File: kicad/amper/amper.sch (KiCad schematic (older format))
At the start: 54 parts, among them J1 Conn_02x05_Odd_Even, J2 Conn_02x05_Odd_Even, J3 Conn_02x05_Odd_Even, J4 USB_C_Receptacle_USB2.0, J5 Conn_01x03, J6 Conn_01x04, J7 Conn_01x05, Q1 FDS9435A, Q2 FDS9435A, SW1 SW_Push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

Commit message: misc corrections
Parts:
- J4: symbol Connector:USB_C_Receptacle_USB2.0 -> amper-symbols:USB_C_Receptacle_USB2.0_shield
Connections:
- no-connect marks 22 -> 25
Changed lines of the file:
@@
 L power:GND #PWR016
 U 1 1 6234E5E5
-P 9050 5200
-F 0 "#PWR016" H 9050 4950 50  0001 C CNN
-F 1 "GND" H 9055 5027 50  0000 C CNN
-F 2 "" H 9050 5200 50  0001 C CNN
-F 3 "" H 9050 5200 50  0001 C CNN
-	1    9050 5200
-	1    0    0    -1
-$EndComp
-Wire Wire Line
-	9050 5200 9050 5100
+P 9150 5200
+F 0 "#PWR016" H 9150 4950 50  0001 C CNN
+F 1 "GND" H 9155 5027 50  0000 C CNN
+F 2 "" H 9150 5200 50  0001 C CNN
+F 3 "" H 9150 5200 50  0001 C CNN
+	1    9150 5200
+	1    0    0    -1
+$EndComp
+Wire Wire Line
+	9150 5200 9150 5100
 $Comp
 L Device:CP1 C5
@@
 NoConn ~ 9650 4300
 $Comp
-L Connector:USB_C_Receptacle_USB2.0 J4
+L amper-symbols:USB_C_Receptacle_USB2.0_shield J4
 U 1 1 626A33B5
 P 9050 4200
@@
 Wire Wire Line
 	1400 2000 1400 2100
+NoConn ~ 8850 5100
+NoConn ~ 8950 5100
+NoConn ~ 9050 5100
 $EndSCHEMATC

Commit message: almost finished first path at board rev b, still a little work to do around logos, text and plane continuity
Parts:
- added J8, J9: Conn_01x09, Connector_PinSocket_2.54mm:PinSocket_1x09_P2.54mm_Vertical, symbol Connector_Generic:Conn_01x09
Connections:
- net AtProg: now also J9.4 (Pin_4)
- net ResultAdc: now also J8.7 (Pin_7)
- net SourceADn: now also J9.7 (Pin_7)
- net SourceAOut: now also J9.3 (Pin_3)
- net SourceAPwm: now also J9.1 (Pin_1)
- net SourceAUp: now also J9.8 (Pin_8)
- net SourceBDn: now also J9.5 (Pin_5)
- net SourceBOut: now also J9.2 (Pin_2)
- net SourceBPwm: now also J9.9 (Pin_9)
- net SourceBUp: now also J9.6 (Pin_6)
- net Tm1637Clk: now also J8.9 (Pin_9)
- net Tm1637Dio: now also J8.8 (Pin_8)
- net UartRx: now also J8.3 (Pin_3)
- net UartTx: now also J8.2 (Pin_2)
- net at U7.10 (PB1): now also J8.1 (Pin_1)
- net at U7.5 (PA7): now also J8.6 (Pin_6)
- net at U7.6 (PB5): now also J8.5 (Pin_5)
- net at U7.7 (PB4): now also J8.4 (Pin_4)
- no-connect marks 25 -> 21
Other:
- note removed: "Expose these traces\nfor ease of bodging"
- moved on the sheet: C12, U7
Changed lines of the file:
@@
 L amper-symbols:ATtiny1606-S U7
 U 1 1 62224E78
-P 9850 2000
-F 0 "U7" H 9850 2965 50  0000 C CNN
-F 1 "ATtiny1606-S" H 9850 2874 50  0000 C CNN
-F 2 "Package_SO:SOIC-20W_7.5x12.8mm_P1.27mm" H 9850 1650 50  0001 C CIN
-F 3 "http://ww1.microchip.com/downloads/en/DeviceDoc/ATtiny806_1606_Data_Sheet_40002029A.pdf" H 9850 2000 50  0001 C CNN
-	1    9850 2000
-	1    0    0    -1
-$EndComp
-Wire Wire Line
-	10450 1300 10550 1300
+P 9300 2000
+F 0 "U7" H 9300 2965 50  0000 C CNN
+F 1 "ATtiny1606-S" H 9300 2874 50  0000 C CNN
+F 2 "Package_SO:SOIC-20W_7.5x12.8mm_P1.27mm" H 9300 1650 50  0001 C CIN
+F 3 "http://ww1.microchip.com/downloads/en/DeviceDoc/ATtiny806_1606_Data_Sheet_40002029A.pdf" H 9300 2000 50  0001 C CNN
+	1    9300 2000
+	1    0    0    -1
+$EndComp
+Wire Wire Line
+	9900 1300 10000 1300
 $Comp
 L power:+5V #PWR017
 U 1 1 622DD6E8
-P 9150 850
-F 0 "#PWR017" H 9150 700 50  0001 C CNN
-F 1 "+5V" H 9165 1023 50  0000 C CNN
-F 2 "" H 9150 850 50  0001 C CNN
-F 3 "" H 9150 850 50  0001 C CNN
-	1    9150 850
-	1    0    0    -1
-$EndComp
-Wire Wire Line
-	9150 1300 9250 1300
+P 8600 850
+F 0 "#PWR017" H 8600 700 50  0001 C CNN
+F 1 "+5V" H 8615 1023 50  0000 C CNN
+F 2 "" H 8600 850 50  0001 C CNN
+F 3 "" H 8600 850 50  0001 C CNN
+	1    8600 850
+	1    0    0    -1
+$EndComp
+Wire Wire Line
+	8600 1300 8700 1300
 $Comp
 L power:GND #PWR022
 U 1 1 622EC3F9
-P 10750 950
-F 0 "#PWR022" H 10750 700 50  0001 C CNN
-F 1 "GND" H 10755 777 50  0000 C CNN
-F 2 "" H 10750 950 50  0001 C CNN
-F 3 "" H 10750 950 50  0001 C CNN
-	1    10750 950
-	1    0    0    -1
-$EndComp
-Wire Wire Line
-	10550 1300 10550 950
-Wire Wire Line
-	10750 850  10750 950
-Text Label 10500 1700 0    50   ~ 0
+P 10200 950
+F 0 "#PWR022" H 10200 700 50  0001 C CNN
+F 1 "GND" H 10205 777 50  0000 C CNN
+F 2 "" H 10200 950 50  0001 C CNN
+F 3 "" H 10200 950 50  0001 C CNN
+	1    10200 950
+	1    0    0    -1
+$EndComp
+Wire Wire Line
+	10000 1300 10000 950
+Wire Wire Line
+	10200 850  10200 950
+Text Label 9950 1700 0    50   ~ 0
 AtProg
-Text Label 10500 1600 0    50   ~ 0
+Text Label 9950 1600 0    50   ~ 0
 SourceAOut
-Text Label 10500 1500 0    50   ~ 0
+Text Label 9950 1500 0    50   ~ 0
 SourceBOut
-Text Label 10500 1400 0    50   ~ 0
+Text Label 9950 1400 0    50   ~ 0
 SourceAPwm
-Text Label 9200 1400 2    50   ~ 0
+Text Label 8650 1400 2    50   ~ 0
 Tm1637Clk
-Text Label 9200 1500 2    50   ~ 0
+Text Label 8650 1500 2    50   ~ 0
 Tm1637Dio
-Text Label 9200 1600 2    50   ~ 0
+Text Label 8650 1600 2    50   ~ 0
 ResultAdc
-Text Label 10500 2200 0    50   ~ 0
+Text Label 9950 2200 0    50   ~ 0
 SourceBPwm
-Text Label 9150 2100 2    50   ~ 0
+Text Label 8600 2100 2    50   ~ 0
 UartTx
-Text Label 9150 2000 2    50   ~ 0
+Text Label 8600 2000 2    50   ~ 0
 UartRx
-Text Label 10500 2100 0    50   ~ 0
+Text Label 9950 2100 0    50   ~ 0
 SourceAUp
-Text Label 10500 2000 0    50   ~ 0
+Text Label 9950 2000 0    50   ~ 0
 SourceADn
-Text Label 10500 1900 0    50   ~ 0
+Text Label 9950 1900 0    50   ~ 0
 SourceBUp
-Text Label 10500 1800 0    50   ~ 0
+Text Label 9950 1800 0    50   ~ 0
 SourceBDn
 $Comp
@@
 Wire Wire Line
 	10600 4650 10700 4650
-Wire Wire Line
-	9150 2100 9250 2100
-Wire Wire Line
-	9150 2000 9250 2000
-Wire Wire Line
-	9200 1400 9250 1400
-Wire Wire Line
-	9200 1500 9250 1500
-Wire Wire Line
-	9200 1600 9250 1600
-NoConn ~ 9250 1700
-NoConn ~ 9250 1800
-NoConn ~ 9250 1900
-NoConn ~ 9250 2200
-Wire Wire Line
-	10450 1400 10500 1400
-Wire Wire Line
-	10450 1500 10500 1500
-Wire Wire Line
-	10500 1600 10450 1600
-Wire Wire Line
-	10450 1700 10500 1700
-Wire Wire Line
-	10500 1800 10450 1800
-Wire Wire Line
-	10450 1900 10500 1900
-Wire Wire Line
-	10500 2000 10450 2000
-Wire Wire Line
-	10450 2100 10500 2100
-Wire Wire Line
-	10500 2200 10450 2200
-Text Notes 9100 2650 0    100  ~ 0
-Expose these traces\nfor ease of bodging
-Wire Notes Line
-	11000 2700 8750 2700
-Wire Notes Line
-	8750 550  11000 550
 $Comp
 L Connector_Generic:Conn_01x05 J7
@@
 Wire Wire Line
 	10700 5600 10050 5600
-Text Notes 850  4850 0    100  ~ 0
-Expose these traces\nfor ease of bodging
 $Comp
 L power:+5V #PWR018
@@
 Wire Wire Line
 	4250 4500 4550 4500
-Wire Notes Line
-	700  4400 4750 4400
-Wire Notes Line
-	700  6250 4750 6250
-Wire Notes Line
-	4750 4400 4750 6250
-Wire Notes Line
-	700  4400 700  6250
 $Comp
 L Connector_Generic:Conn_02x05_Odd_Even J3
@@
 L Device:C C12
 U 1 1 62E8013E
-P 10300 950
-F 0 "C12" V 10048 950 50  0000 C CNN
-F 1 "100n" V 10139 950 50  0000 C CNN
-F 2 "Capacitor_SMD:C_0603_1608Metric_Pad1.05x0.95mm_HandSolder" H 10338 800 50  0001 C CNN
-F 3 "~" H 10300 950 50  0001 C CNN
-	1    10300 950
+P 9750 950
+F 0 "C12" V 9498 950 50  0000 C CNN
+F 1 "100n" V 9589 950 50  0000 C CNN
+F 2 "Capacitor_SMD:C_0603_1608Metric_Pad1.05x0.95mm_HandSolder" H 9788 800 50  0001 C CNN
+F 3 "~" H 9750 950 50  0001 C CNN
+	1    9750 950
 	0    1    1    0
 $EndComp
 Wire Wire Line
-	10550 850  10750 850
-Wire Wire Line
-	10450 950  10550 950
-Connection ~ 10550 950
-Wire Wire Line
-	10550 950  10550 850
-Wire Wire Line
-	10150 950  9150 950
-Wire Wire Line
-	9150 950  9150 1300
-Wire Wire Line
-	9150 950  9150 850
-Connection ~ 9150 950
-Wire Notes Line
-	8750 550  8750 2700
-Wire Notes Line
-	11000 550  11000 2700
+	10000 850  10200 850
+Wire Wire Line
+	9900 950  10000 950
+Connection ~ 10000 950
+Wire Wire Line
+	10000 950  10000 850
+Wire Wire Line
+	9600 950  8600 950
+Wire Wire Line
+	8600 950  8600 1300
+Wire Wire Line
+	8600 950  8600 850
+Connection ~ 8600 950
 Wire Wire Line
 	1000 3250 1400 3250
@@
 NoConn ~ 8950 5100
 NoConn ~ 9050 5100
+$Comp
+L Connector_Generic:Conn_01x09 J8
+U 1 1 634F05AF
+P 8000 1800
+F 0 "J8" H 8000 1150 50  0000 C CNN
+F 1 "Conn_01x09" H 8000 1250 50  0000 C CNN
+F 2 "Connector_PinSocket_2.54mm:PinSocket_1x09_P2.54mm_Vertical" H 8000 1800 50  0001 C CNN
+F 3 "~" H 8000 1800 50  0001 C CNN
+	1    8000 1800
+	-1   0    0    1
+$EndComp
+Wire Wire Line
+	8200 1400 8700 1400
+Wire Wire Line
+	8200 1500 8700 1500
+Wire Wire Line
+	8200 1600 8700 1600
+Wire Wire Line
+	8200 2000 8700 2000
+Wire Wire Line
+	8200 2100 8700 2100
+Wire Wire Line
+	9900 2200 10400 2200
+Wire Wire Line
+	8200 1900 8700 1900
+Wire Wire Line
+	8700 1800 8200 1800
+Wire Wire Line
+	8200 1700 8700 1700
+$Comp
+L Connector_Generic:Conn_01x09 J9
+U 1 1 635FB8AF
+P 10600 1800
+F 0 "J9" H 10600 2450 50  0000 C CNN
+F 1 "Conn_01x09" H 10600 2350 50  0000 C CNN
+F 2 "Connector_PinSocket_2.54mm:PinSocket_1x09_P2.54mm_Vertical" H 10600 1800 50  0001 C CNN
+F 3 "~" H 10600 1800 50  0001 C CNN
+	1    10600 1800
+	1    0    0    -1
+$EndComp
+Wire Wire Line
+	8200 2200 8700 2200
+Wire Wire Line
+	9900 2100 10400 2100
+Wire Wire Line
+	9900 2000 10400 2000
+Wire Wire Line
+	9900 1900 10400 1900
+Wire Wire Line
+	9900 1800 10400 1800
+Wire Wire Line
+	9900 1700 10400 1700
+Wire Wire Line
+	9900 1600 10400 1600
+Wire Wire Line
+	9900 1500 10400 1500
+Wire Wire Line
+	9900 1400 10400 1400
 $EndSCHEMATC

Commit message: rev B as fabbed
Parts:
- J8, J9: footprint Connector_PinSocket_2.54mm:PinSocket_1x09_P2.54mm_Vertical -> amper:PinSocket_1x09_P2.54mm_Vertical_no_silk
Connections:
- net AtProg: now also J9.6 (Pin_6); no longer J9.4 (Pin_4)
- net SourceADn: now also J9.3 (Pin_3); no longer J9.7 (Pin_7)
- net SourceAOut: now also J9.7 (Pin_7); no longer J9.3 (Pin_3)
- net SourceAPwm: now also J9.9 (Pin_9); no longer J9.1 (Pin_1)
- net SourceAUp: now also J9.2 (Pin_2); no longer J9.8 (Pin_8)
- net SourceBOut: now also J9.8 (Pin_8); no longer J9.2 (Pin_2)
- net SourceBPwm: now also J9.1 (Pin_1); no longer J9.9 (Pin_9)
- net SourceBUp: now also J9.4 (Pin_4); no longer J9.6 (Pin_6)
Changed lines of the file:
@@
 F 0 "J8" H 8000 1150 50  0000 C CNN
 F 1 "Conn_01x09" H 8000 1250 50  0000 C CNN
-F 2 "Connector_PinSocket_2.54mm:PinSocket_1x09_P2.54mm_Vertical" H 8000 1800 50  0001 C CNN
+F 2 "amper:PinSocket_1x09_P2.54mm_Vertical_no_silk" H 8000 1800 50  0001 C CNN
 F 3 "~" H 8000 1800 50  0001 C CNN
 	1    8000 1800
@@
 U 1 1 635FB8AF
 P 10600 1800
-F 0 "J9" H 10600 2450 50  0000 C CNN
-F 1 "Conn_01x09" H 10600 2350 50  0000 C CNN
-F 2 "Connector_PinSocket_2.54mm:PinSocket_1x09_P2.54mm_Vertical" H 10600 1800 50  0001 C CNN
+F 0 "J9" H 10600 1150 50  0000 C CNN
+F 1 "Conn_01x09" H 10600 1250 50  0000 C CNN
+F 2 "amper:PinSocket_1x09_P2.54mm_Vertical_no_silk" H 10600 1800 50  0001 C CNN
 F 3 "~" H 10600 1800 50  0001 C CNN
 	1    10600 1800
-	1    0    0    -1
+	1    0    0    1
 $EndComp
 Wire Wire Line

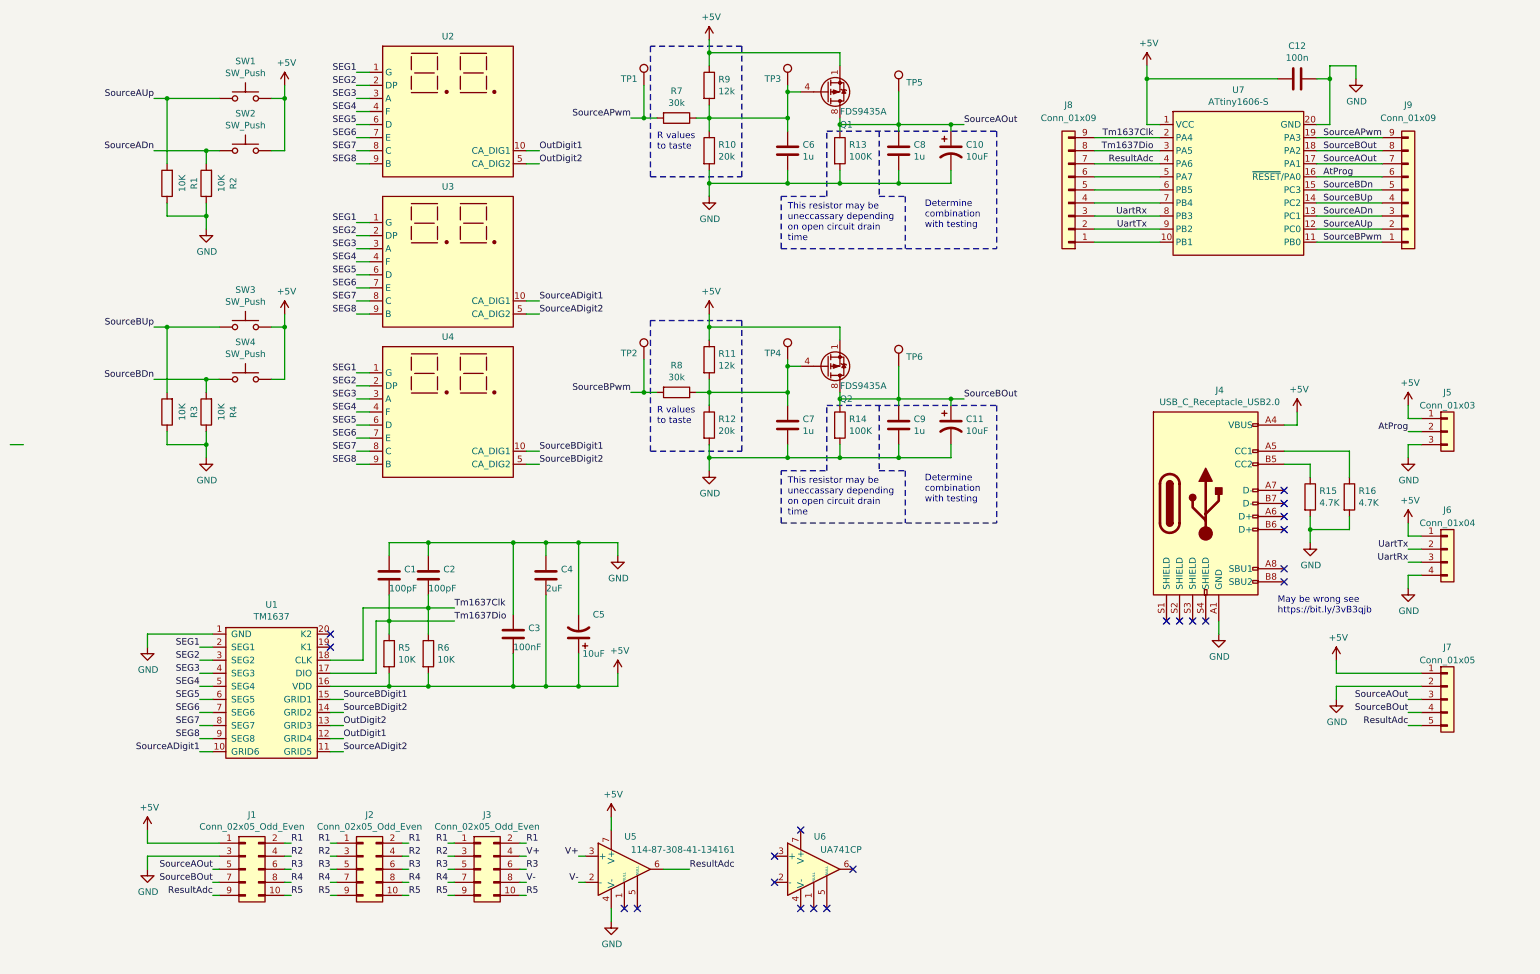
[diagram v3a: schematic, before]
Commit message: Updated power supplies to schematic, reorganised schematic
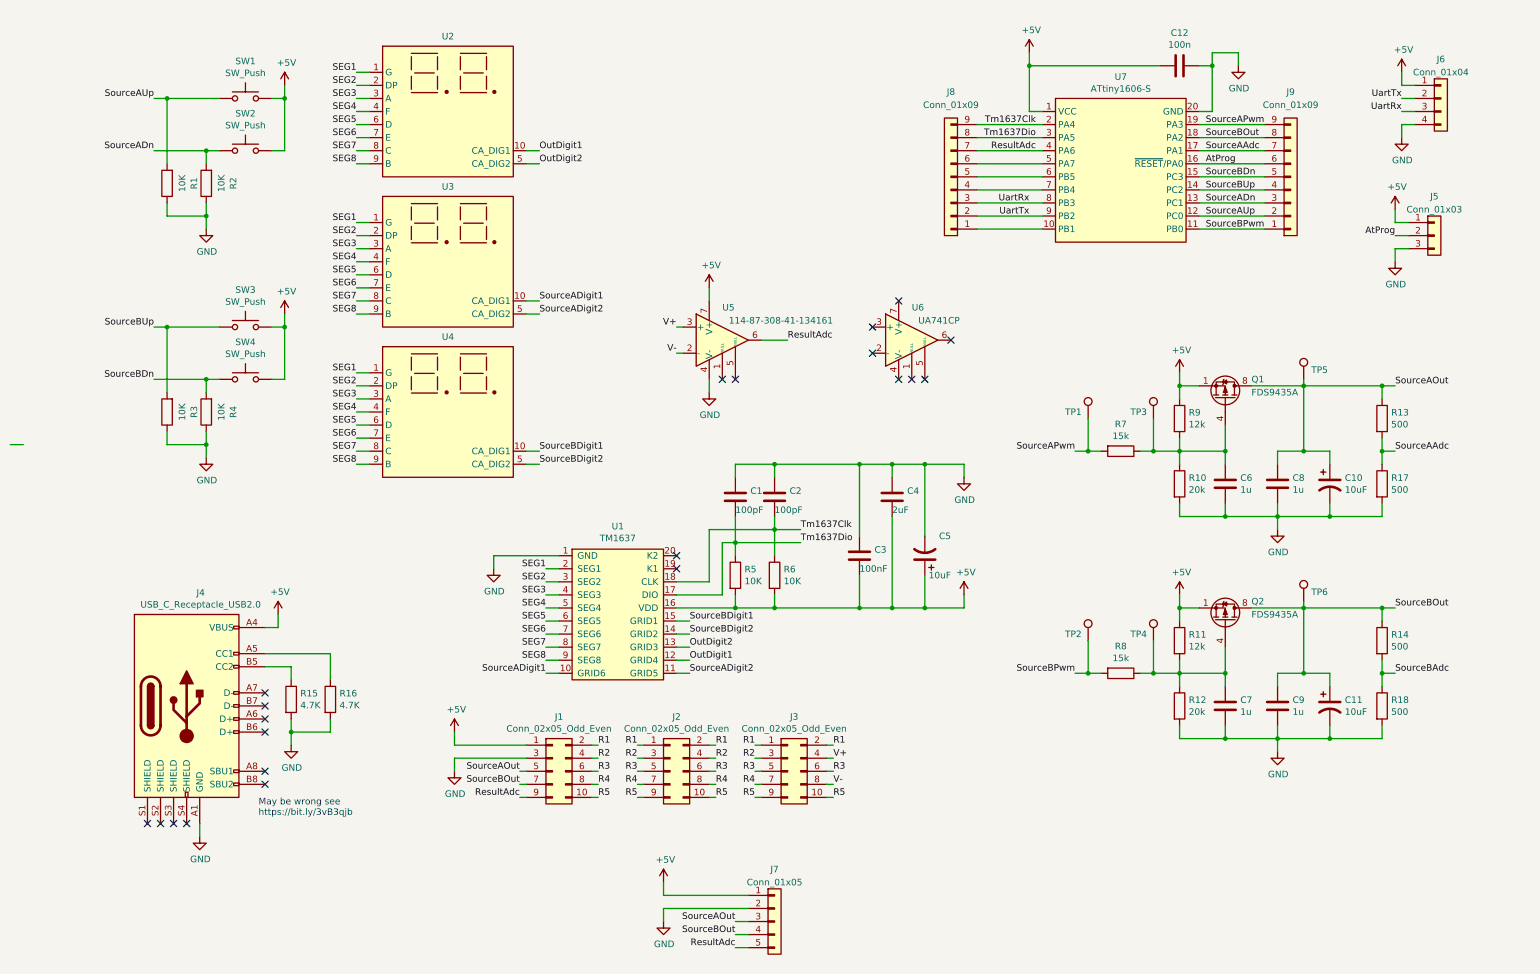
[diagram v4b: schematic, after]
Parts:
- added R17, R18: 500, symbol Device:R
- R13, R14: value 100K -> 500; footprint Resistor_SMD:R_0603_1608Metric_Pad1.05x0.95mm_HandSolder -> (none); Vendor Already Have -> (none)
- R7, R8: value 30k -> 15k
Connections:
- net GND: now also R17.2, R18.2; no longer R13.2, R14.2
- net SourceAOut: no longer J9.7 (Pin_7), U7.17 (PA1)
- new net SourceAAdc: J9.7 (Pin_7), R13.2, R17.1, U7.17 (PA1)
- new net SourceBAdc: R14.2, R18.1
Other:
- note removed: "Determine\ncombination\nwith testing"
- note removed: "R values\nto taste"
- note removed: "This resistor may be\nuneccassary depending\non open circuit drain\ntime"
- moved on the sheet: C1, C10, C12, C2, C3, C4, C5, C6, C8, J1, J2, J3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

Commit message: moved components to make better use of schematic
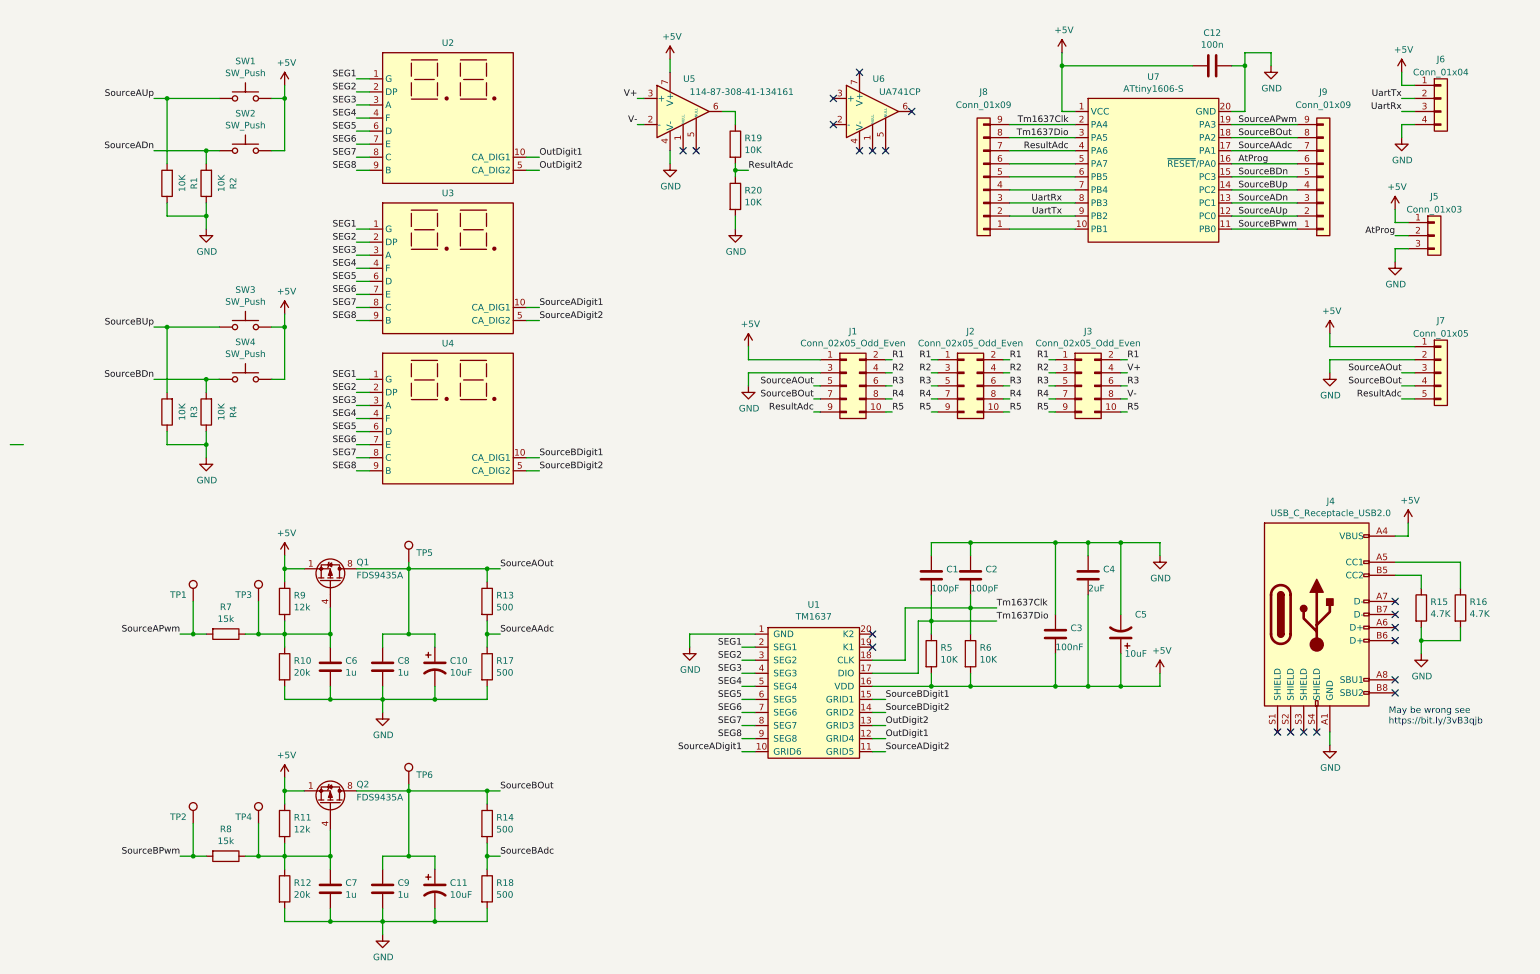
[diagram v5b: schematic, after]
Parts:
- added R19, R20: 10K, Resistor_SMD:R_0603_1608Metric_Pad1.05x0.95mm_HandSolder, symbol Device:R
- R13, R14, R17, R18: footprint (none) -> Resistor_SMD:R_0603_1608Metric_Pad1.05x0.95mm_HandSolder
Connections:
- net GND: now also R20.2
- net ResultAdc: now also R19.2, R20.1; no longer U5.6
- new net: R19.1, U5.6
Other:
- moved on the sheet: C1, C10, C11, C12, C2, C3, C4, C5, C6, C7, C8, C9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

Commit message: Updated opamp
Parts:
- removed U6: UA741CP, symbol Amplifier_Operational:LM741
- U5: symbol Amplifier_Operational:LM741 -> amper-symbols:MCP602-single
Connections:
- net +5V: now also U5.6 (NULL), U5.8 (V+); no longer U5.7 (V+)
- net GND: now also U5.5 (NULL)
- net at U5.1: now also R19.1
- no-connect marks 21 -> 12
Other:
- moved on the sheet: J1, J2, J3, R19, R20
